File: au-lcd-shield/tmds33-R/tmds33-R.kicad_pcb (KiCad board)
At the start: 2 copper layers, 65 x 45 mm, 14 parts, among them IC1 ME6206A15M3G, J1 Power, J2 Backlight, J4 Conn_02x09_Odd_Even, U1 UA78M33CDCYR

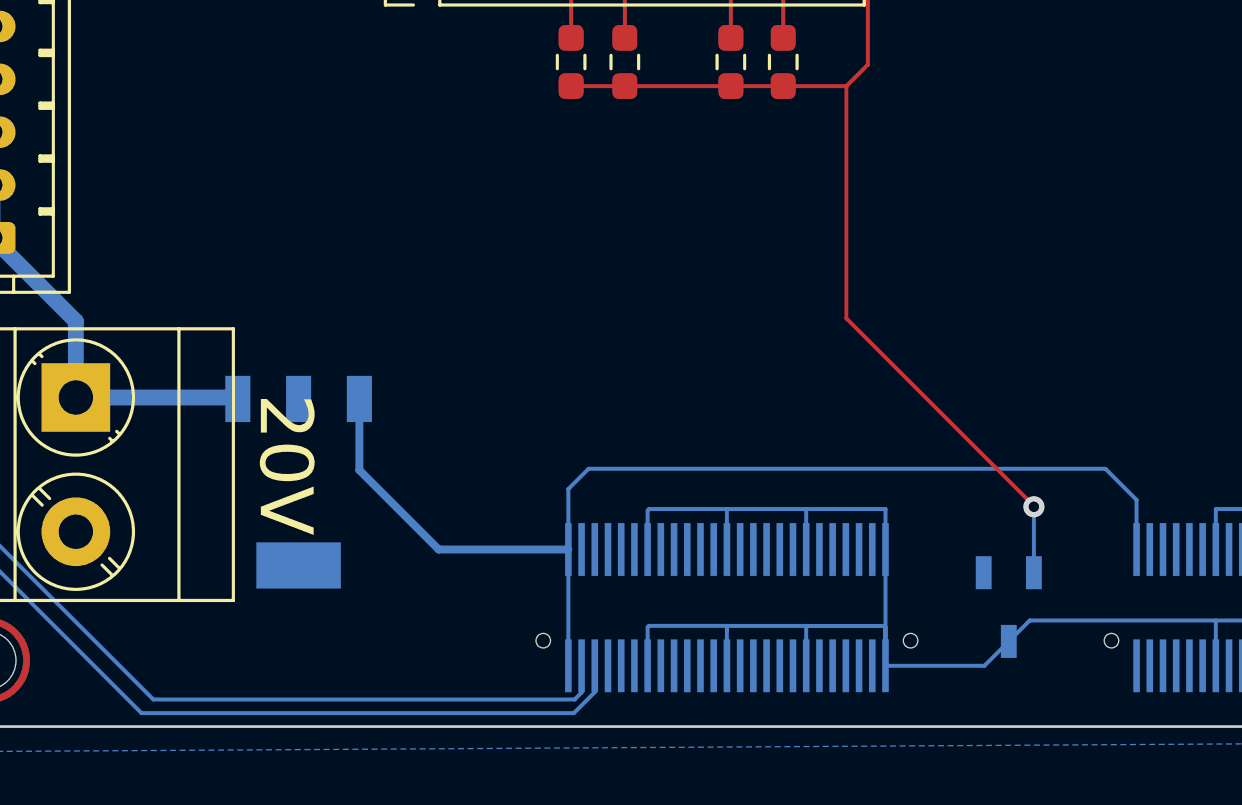
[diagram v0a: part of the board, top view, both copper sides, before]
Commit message: add filtering caps for ldo's
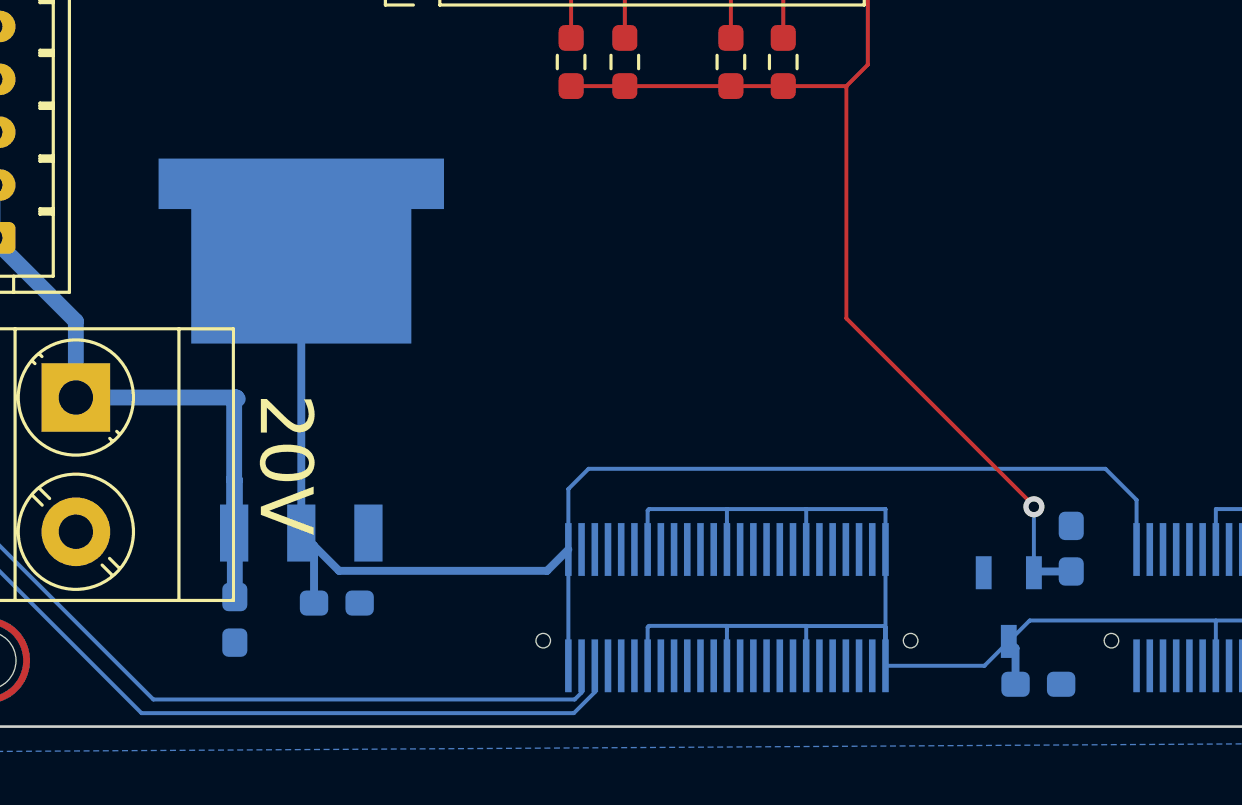
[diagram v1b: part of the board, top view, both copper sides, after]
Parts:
- removed U1: UA78M33CDCYR, SamacSys_Parts:SOT230P700X180-4N
- added C1: 10uF, Capacitor_SMD:C_0603_1608Metric_Pad1.08x0.95mm_HandSolder, B.Cu at (127.2, 117.9)
- added C2: 10uF, Capacitor_SMD:C_0603_1608Metric_Pad1.08x0.95mm_HandSolder, B.Cu at (123.3, 118.5)
- added C3: 1uF, Capacitor_SMD:C_0603_1608Metric_Pad1.08x0.95mm_HandSolder, B.Cu at (155.0, 115.8)
- added C4: 1uF, Capacitor_SMD:C_0603_1608Metric_Pad1.08x0.95mm_HandSolder, B.Cu at (153.7, 120.9)
- added IC3: LM1085ISX-5.0_NOPB, SamacSys_Parts:KTT0003B, B.Cu at (125.8, 102.5)
- renumbered Re to R1
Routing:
- net +5V: track 42.7 -> 55.4 mm
- net VCC: track 15.5 -> 25.1 mm
- net +3.3V: track 207.1 -> 208.9 mm
- net +1V5: track 52.9 -> 54.3 mm

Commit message: pcb v1.0
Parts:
- removed IC1: ME6206A15M3G, SamacSys_Parts:SOT95P285X145-3N
- removed IC3: LM1085ISX-5.0_NOPB, SamacSys_Parts:KTT0003B
- added U1: ME6206A15M3G, Library:SOT95P285X145-3N, B.Cu at (151.6, 118.0)
- added U2: 78M05, Package_TO_SOT_SMD:TO-252-2, B.Cu at (127.3, 113.5)
- moved C2 12.4 mm to (125.7, 106.3), turned to 0 degrees
- moved C1 11.7 mm to (129.0, 106.3), turned to 180 degrees
- moved C3 0.92 mm to (154.5, 115.0), turned to 0 degrees
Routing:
- net +5V: track 55.4 -> 89.4 mm, vias 0 -> 4
- net VCC: track 25.1 -> 20.0 mm
- net +3.3V: track 208.9 -> 209.9 mm
- net +1V5: track 54.3 -> 55.2 mm
- net GND: vias 0 -> 230
- added copper zone on F.Cu, net GND
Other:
- board text added: "+"
- board text added: "-"
